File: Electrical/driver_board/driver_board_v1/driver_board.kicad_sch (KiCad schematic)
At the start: 34 parts, among them J1 Screw_Terminal_01x02, J2 Screw_Terminal_01x02, J3 Screw_Terminal_01x04, J4 Conn_01x04, J5 Conn_01x04, J6 Conn_01x04, J7 Conn_01x04, J8 Conn_01x04, J9 Conn_01x04, SW1 SW_DIP_x04, SW2 SW_DIP_x04, SW3 SW_DIP_x04, SW4 SW_DIP_x04, SW5 SW_DIP_x04, SW6 SW_DIP_x04, U1 ESP32-WROOM-32

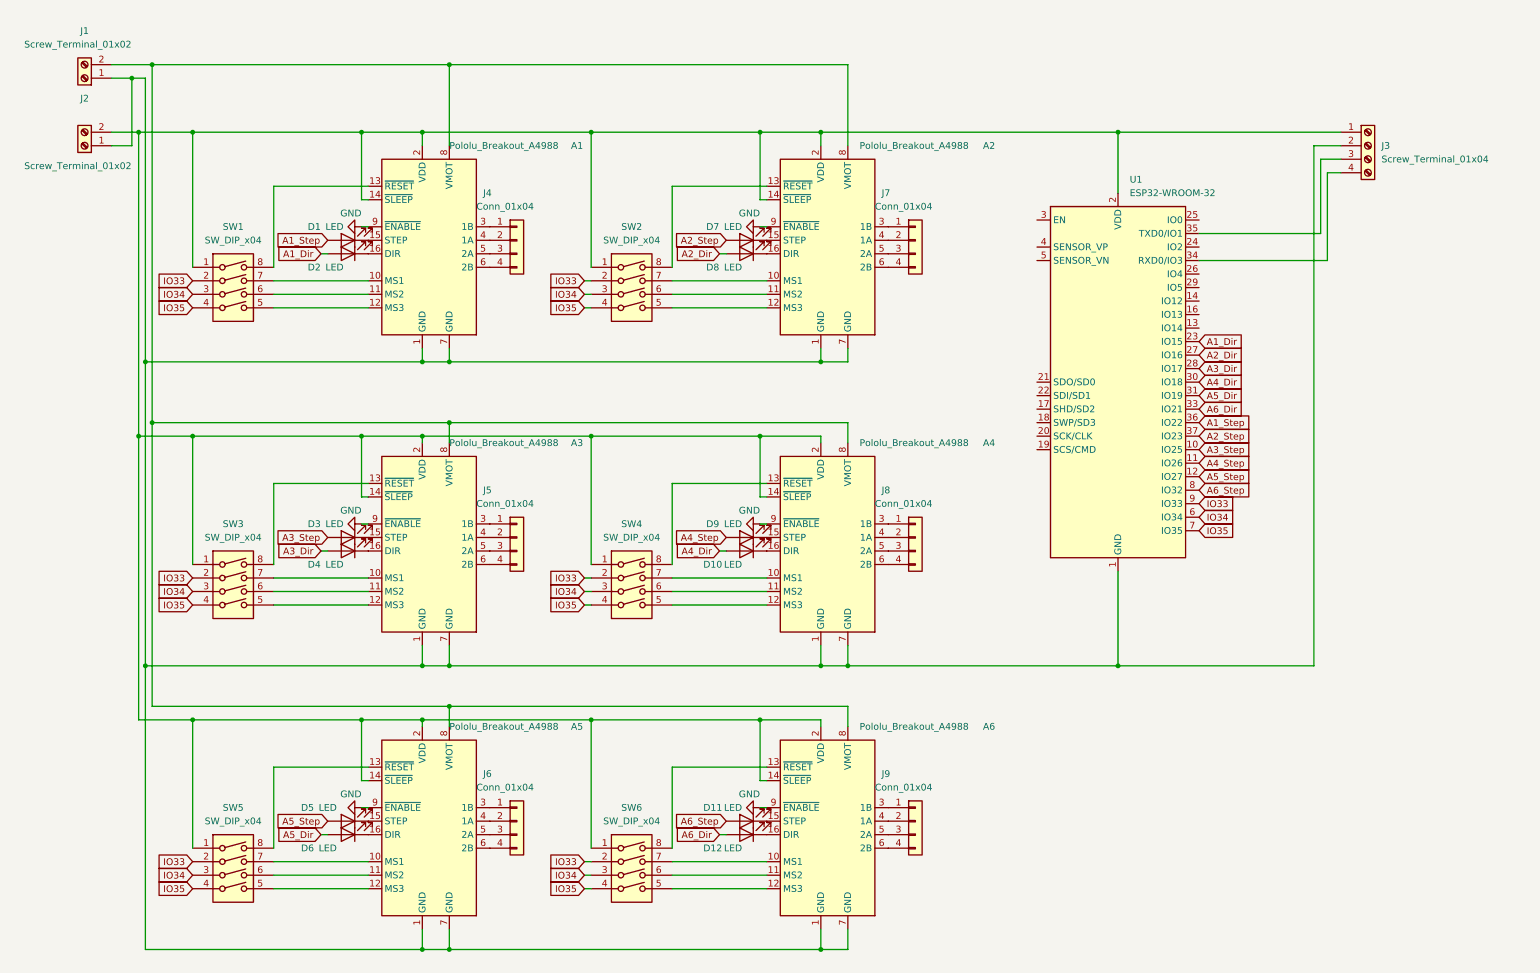
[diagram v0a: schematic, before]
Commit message: Driver_Board schematic changes
Added smoothing capacitors
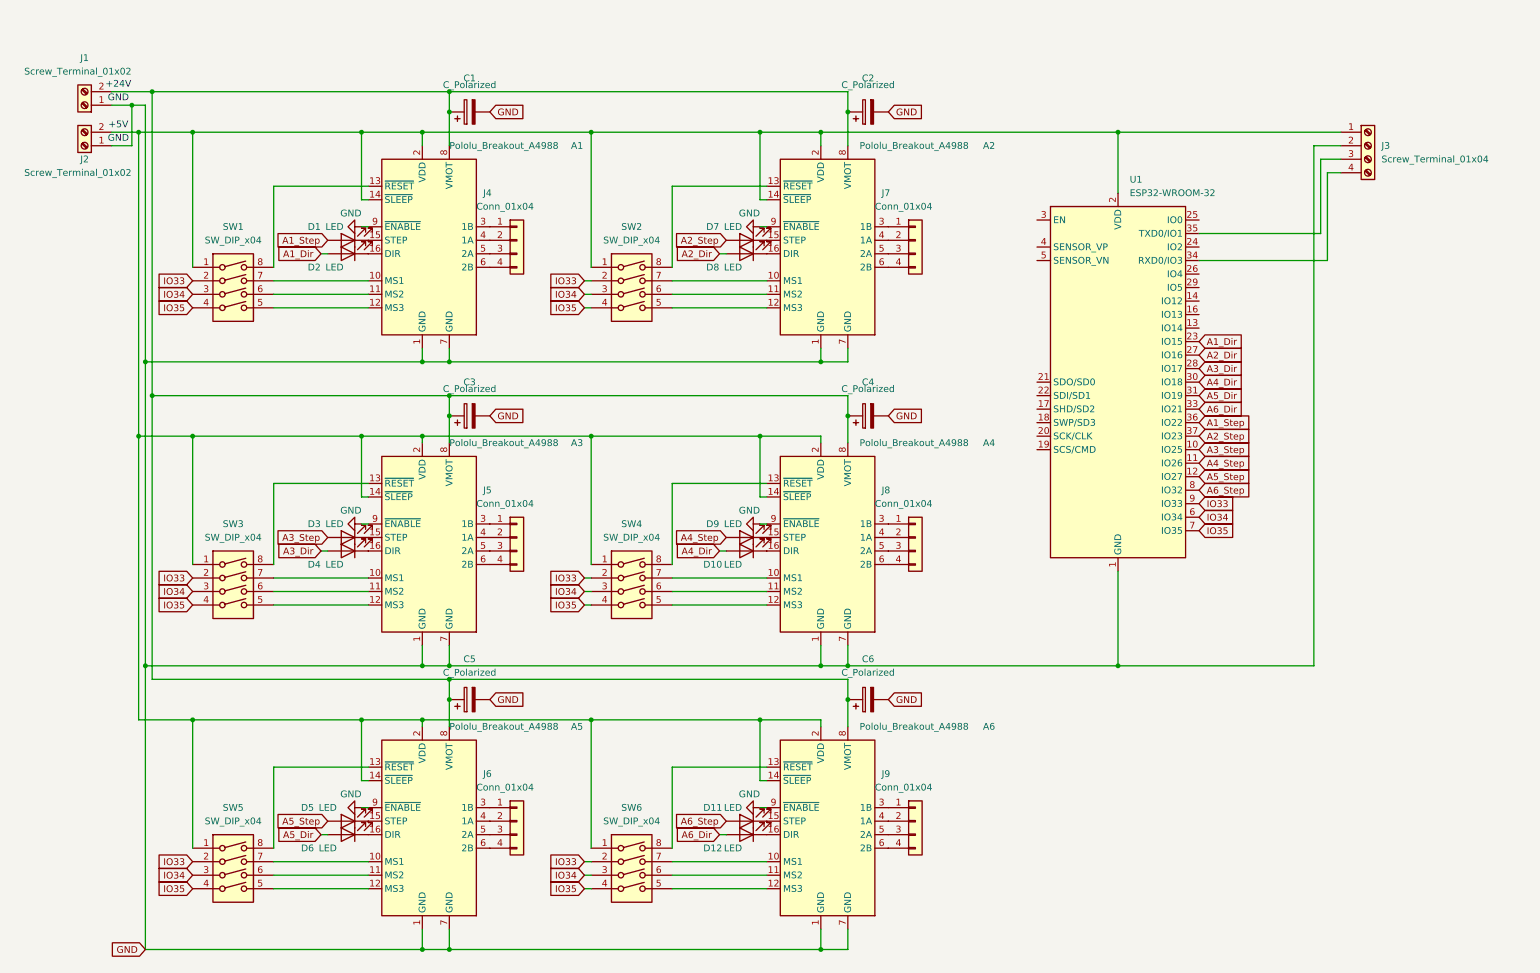
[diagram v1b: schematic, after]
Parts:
- added C1, C2, C3, C4, C5, C6: C_Polarized, symbol Device:C_Polarized
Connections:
- net GND: now also A1.1 (GND), A1.7 (GND), A2.1 (GND), A2.7 (GND), A3.1 (GND), A3.7 (GND), A4.1 (GND), A4.7 (GND), A5.1 (GND), A5.7 (GND), A6.1 (GND), A6.7 (GND), J1.1 (Pin_1), J2.1 (Pin_1), J3.2 (Pin_2), U1.1 (GND), U1.15 (GND), U1.38 (GND), U1.39 (GND), C1.2, C2.2, C3.2, C4.2, C5.2, C6.2
- net at A1.8 (VMOT), A2.8 (VMOT), A3.8 (VMOT)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: now also C1.1, C2.1, C3.1, C4.1, C5.1, C6.1
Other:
- note added: "+24V"
- note added: "+5V"
- note added: "GND"
- moved on the sheet: J1

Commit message: Updated driver board v1
New dip switch allignment and assigned first footprints
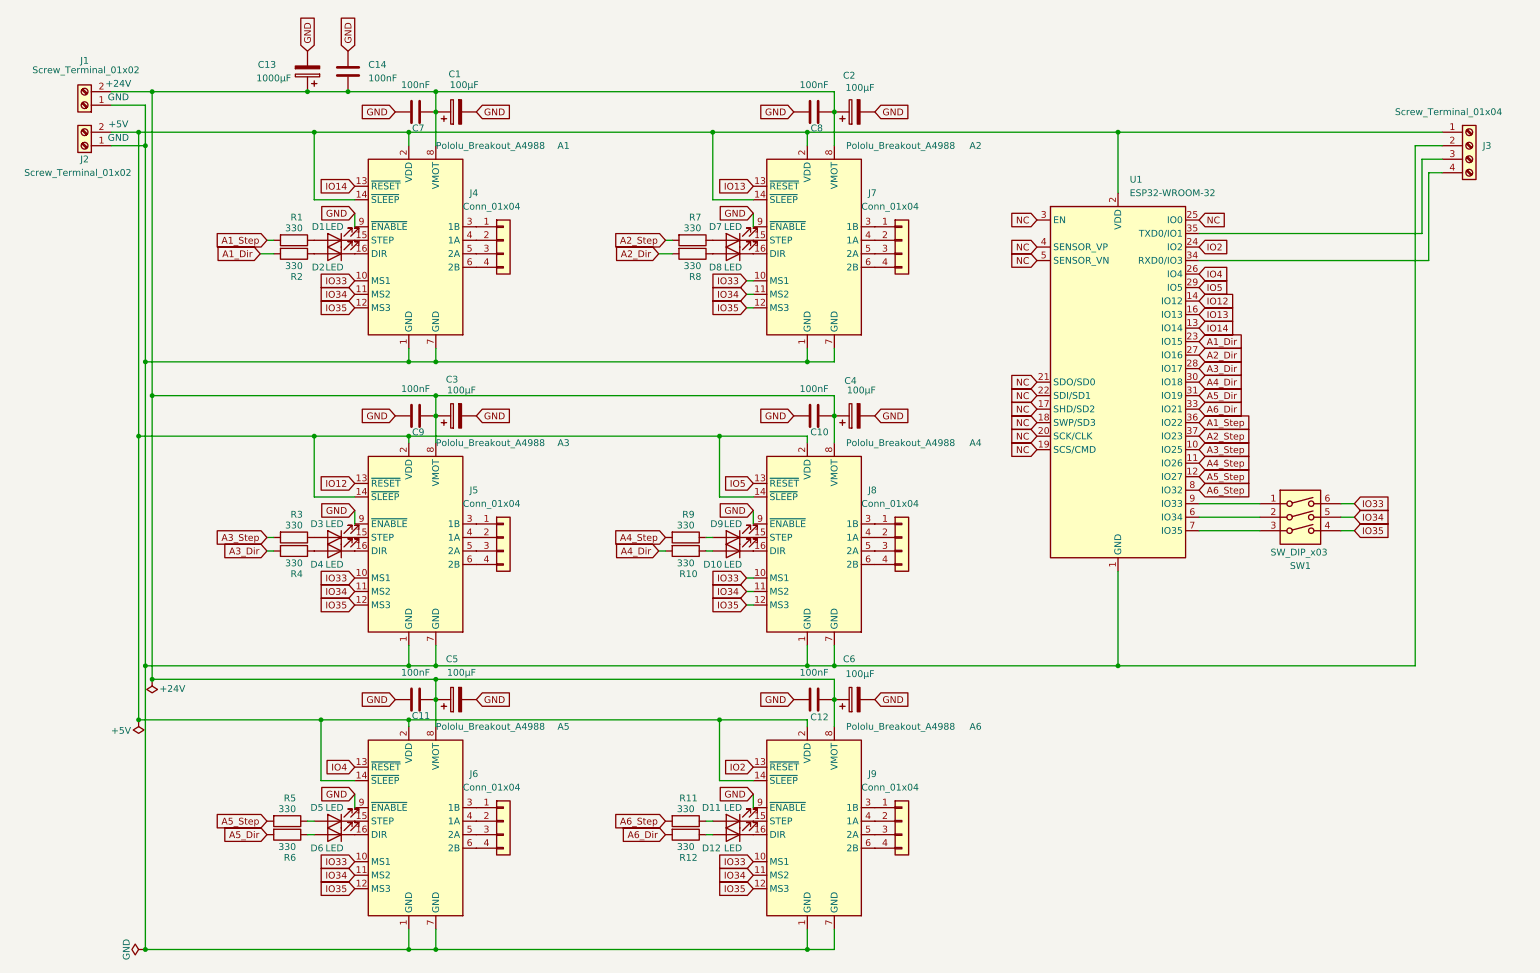
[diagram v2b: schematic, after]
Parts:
- removed SW1, SW2, SW3, SW4, SW5, SW6: SW_DIP_x04, symbol Switch:SW_DIP_x04
- added C10, C11, C12, C14, C7, C8, C9: 100nF, symbol Device:C
- added C13: 1000µF, symbol Device:C_Polarized
- added R1, R10, R11, R12, R2, R3, R4, R5, R6, R7, R8, R9: 330, symbol Device:R
- added SW1: SW_DIP_x03, symbol Switch:SW_DIP_x03
- C1, C2, C3, C4, C5, C6: value C_Polarized -> 100µF
- D1, D10, D11, D12, D2, D3, D4, D5, D6, D7, D8, D9: footprint (none) -> LED_SMD:LED_0603_1608Metric
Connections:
- net A1_Dir: now also R2.2; no longer D2.2 (A)
- net A1_Step: now also R1.2; no longer D1.2 (A)
- net A2_Dir: now also R8.2; no longer D8.2 (A)
- net A2_Step: now also R7.2; no longer D7.2 (A)
- net A3_Dir: now also R4.2; no longer D4.2 (A)
- net A3_Step: now also R3.2; no longer D3.2 (A)
- net A4_Dir: now also R10.2; no longer D10.2 (A)
- net A4_Step: now also R9.2; no longer D9.2 (A)
- net A5_Dir: now also R6.2; no longer D6.2 (A)
- net A5_Step: now also R5.2; no longer D5.2 (A)
- net A6_Dir: now also R12.2; no longer D12.2 (A)
- net A6_Step: now also R11.2; no longer D11.2 (A)
- net GND: now also C10.1, C11.1, C12.1, C13.2, C14.2, C7.1, C8.1, C9.1; no longer A1.1 (GND), A1.7 (GND), A2.1 (GND), A2.7 (GND), A3.1 (GND), A3.7 (GND), A4.1 (GND), A4.7 (GND), A5.1 (GND), A5.7 (GND), A6.1 (GND), A6.7 (GND), J1.1 (Pin_1), J2.1 (Pin_1), J3.2 (Pin_2), U1.1 (GND), U1.15 (GND), U1.38 (GND), U1.39 (GND)
- net IO33: now also A1.10 (MS1), A2.10 (MS1), A3.10 (MS1), A4.10 (MS1), A5.10 (MS1), A6.10 (MS1), SW1.6; no longer U1.9 (IO33)
- net IO34: now also A1.11 (MS2), A2.11 (MS2), A3.11 (MS2), A4.11 (MS2), A5.11 (MS2), A6.11 (MS2), SW1.5; no longer U1.6 (IO34)
- net IO35: now also A1.12 (MS3), A2.12 (MS3), A3.12 (MS3), A4.12 (MS3), A5.12 (MS3), A6.12 (MS3), SW1.4; no longer U1.7 (IO35)
- net IO12: now reaches A3.13 (~{RESET})
- net IO12: now also U1.14 (IO12)
- net at A1.8 (VMOT), A2.8 (VMOT), A3.8 (VMOT)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: now also C10.2, C11.2, C12.2, C13.1, C14.1, C7.2, C8.2, C9.2
- net IO4: now reaches A5.13 (~{RESET})
- net IO4: now also U1.26 (IO4)
- net IO13: now reaches A2.13 (~{RESET})
- net IO13: now also U1.16 (IO13)
- net IO14: now reaches U1.13 (IO14)
- net IO14: now also A1.13 (~{RESET})
- net NC: now reaches U1.17 (SHD/SD2)
- net NC: now also U1.18 (SWP/SD3), U1.19 (SCS/CMD), U1.20 (SCK/CLK), U1.21 (SDO/SD0), U1.22 (SDI/SD1), U1.25 (IO0), U1.3 (EN), U1.4 (SENSOR_VP), U1.5 (SENSOR_VN)
- net IO2: now reaches U1.24 (IO2)
- net IO2: now also A6.13 (~{RESET})
- net IO5: now reaches U1.29 (IO5)
- net IO5: now also A4.13 (~{RESET})
- new net: A1.1 (GND), A1.7 (GND), A2.1 (GND), A2.7 (GND), A3.1 (GND), A3.7 (GND), A4.1 (GND), A4.7 (GND), A5.1 (GND), A5.7 (GND), A6.1 (GND), A6.7 (GND), J1.1 (Pin_1), J2.1 (Pin_1), J3.2 (Pin_2), U1.1 (GND), U1.15 (GND), U1.38 (GND), U1.39 (GND)
- new net: D5.2 (A), R5.1
- new net: D11.2 (A), R11.1
- new net: D7.2 (A), R7.1
- new net: D12.2 (A), R12.1
- new net: D6.2 (A), R6.1
- new net: D8.2 (A), R8.1
- new net: D10.2 (A), R10.1
- new net: D4.2 (A), R4.1
- new net: D9.2 (A), R9.1
- new net: D2.2 (A), R2.1
- new net: SW1.2, U1.6 (IO34)
- new net: SW1.3, U1.7 (IO35)
- new net: SW1.1, U1.9 (IO33)
- new net: D3.2 (A), R3.1
- new net: D1.2 (A), R1.1
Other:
- moved on the sheet: A1, A2, A3, A4, A5, A6, C1, C2, C3, C4, C5, C6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

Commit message: Minimal ciruit for the STM32F446RET6
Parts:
- removed A1, A2, A3, A4, A5, A6: Pololu_Breakout_A4988, Module:Pololu_Breakout-16_15.2x20.3mm, symbol Driver_Motor:Pololu_Breakout_A4988
- added A1, A2, A3, A4, A5, A6: Pololu_Breakout_A4988, Module:Pololu_Breakout-16_15.2x20.3mm, symbol open_robot_arm_lib:Pololu_Breakout_A4988
- C1, C2, C3, C4, C5, C6: footprint (none) -> Capacitor_SMD:CP_Elec_6.3x7.7
- C10, C11, C12, C13, C14, C7, C8, C9: footprint (none) -> Capacitor_SMD:C_0603_1608Metric
- J1, J2, J3: footprint (none) -> TerminalBlock_Phoenix:TerminalBlock_Phoenix_MKDS-1,5-2-5.08_1x02_P5.08mm_Horizontal
- R1, R10, R11, R12, R2, R3, R4, R5, R6, R7, R8, R9: footprint (none) -> Resistor_SMD:R_0603_1608Metric
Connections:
- net GND: now also J1.1 (Pin_1), J2.1 (Pin_1), J3.2 (Pin_2), U1.1 (GND), U1.15 (GND), U1.38 (GND), U1.39 (GND), A1.1 (GND), A1.7 (GND), A1.9 (~{ENABLE}), A2.1 (GND), A2.7 (GND), A2.9 (~{ENABLE}), A3.1 (GND), A3.7 (GND), A3.9 (~{ENABLE}), A4.1 (GND), A4.7 (GND), A4.9 (~{ENABLE}), A5.1 (GND), A5.7 (GND), A5.9 (~{ENABLE}), A6.1 (GND), A6.7 (GND), A6.9 (~{ENABLE}); no longer C13.2, C14.2
- net IO12: now also A3.13 (~{RESET})
- net IO13: now also A2.13 (~{RESET})
- net IO14: now also A1.13 (~{RESET})
- net IO2: now also A6.13 (~{RESET})
- net IO33: now also A1.10 (MS1), A2.10 (MS1), A3.10 (MS1), A4.10 (MS1), A5.10 (MS1), A6.10 (MS1)
- net IO34: now also A1.11 (MS2), A2.11 (MS2), A3.11 (MS2), A4.11 (MS2), A5.11 (MS2), A6.11 (MS2)
- net IO35: now also A1.12 (MS3), A2.12 (MS3), A3.12 (MS3), A4.12 (MS3), A5.12 (MS3), A6.12 (MS3)
- net IO4: now also A5.13 (~{RESET})
- net IO5: now also A4.13 (~{RESET})
- net +24V: now reaches C1.1, C10.2, C11.2, C12.2, C13.1, C14.1, C2.1, C3.1, C4.1, C5.1, C6.1, C7.2, C8.2, C9.2, J1.2 (Pin_2)
- net +24V: now also A1.8 (VMOT), A2.8 (VMOT), A3.8 (VMOT), A4.8 (VMOT), A5.8 (VMOT), A6.8 (VMOT)
- net at J4.1 (Pin_1): now also A1.3 (1B)
- net at J4.2 (Pin_2): now also A1.4 (1A)
- net at J4.3 (Pin_3): now also A1.5 (2A)
- net at J4.4 (Pin_4): now also A1.6 (2B)
- net +5V: now reaches J2.2 (Pin_2), J3.1 (Pin_1), U1.2 (VDD)
- net +5V: now also A1.14 (~{SLEEP}), A1.2 (VDD), A2.14 (~{SLEEP}), A2.2 (VDD), A3.14 (~{SLEEP}), A3.2 (VDD), A4.14 (~{SLEEP}), A4.2 (VDD), A5.14 (~{SLEEP}), A5.2 (VDD), A6.14 (~{SLEEP}), A6.2 (VDD)
- net at D3.1 (K): now also A3.15 (STEP)
- net at D4.1 (K): now also A3.16 (DIR)
- net at J5.1 (Pin_1): now also A3.3 (1B)
- net at J5.2 (Pin_2): now also A3.4 (1A)
- net at J5.3 (Pin_3): now also A3.5 (2A)
- net at J5.4 (Pin_4): now also A3.6 (2B)
- net at D5.1 (K): now also A5.15 (STEP)
- net at D7.1 (K): now also A2.15 (STEP)
- net at D8.1 (K): now also A2.16 (DIR)
- net at D6.1 (K): now also A5.16 (DIR)
- net at J6.1 (Pin_1): now also A5.3 (1B)
- net at J6.2 (Pin_2): now also A5.4 (1A)
- net at J6.3 (Pin_3): now also A5.5 (2A)
- net at J6.4 (Pin_4): now also A5.6 (2B)
- net at J7.1 (Pin_1): now also A2.3 (1B)
- net at J7.2 (Pin_2): now also A2.4 (1A)
- net at J7.3 (Pin_3): now also A2.5 (2A)
- net at J7.4 (Pin_4): now also A2.6 (2B)
- net at J9.1 (Pin_1): now also A6.3 (1B)
- net at J9.2 (Pin_2): now also A6.4 (1A)
- net at J9.3 (Pin_3): now also A6.5 (2A)
- net at J9.4 (Pin_4): now also A6.6 (2B)
- net at D2.1 (K): now also A1.16 (DIR)
- net at D10.1 (K): now also A4.16 (DIR)
- net at D9.1 (K): now also A4.15 (STEP)
- net at J8.1 (Pin_1): now also A4.3 (1B)
- net at J8.2 (Pin_2): now also A4.4 (1A)
- net at J8.3 (Pin_3): now also A4.5 (2A)
- net at J8.4 (Pin_4): now also A4.6 (2B)
- net at D1.1 (K): now also A1.15 (STEP)
- net at D12.1 (K): now also A6.16 (DIR)
- net at D11.1 (K): now also A6.15 (STEP)
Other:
- added sheet Neuer Zettel (untitled.kicad_sch)
- note removed: "+24V"
- note removed: "+5V"
- note removed: "GND"
- moved on the sheet: C1, C10, C3, C4, C7, C9
